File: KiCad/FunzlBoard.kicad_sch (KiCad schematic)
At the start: 0 parts

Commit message: Add main screw holes
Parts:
- added H1, H10, H2, H3, H4, H5, H6, H7, H8, H9: MountingHole, MountingHole:MountingHole_4.3mm_M4_DIN965, symbol Mechanical:MountingHole

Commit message: Cut out for battery
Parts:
- added D1, D10, D11, D12, D13, D14, D15, D16, D17, D18, D19, D2, D20, D21, D22, D23, D24, D25, D26, D27, D28, D29, D3, D30, D31, D32, D33, D34, D35, D36, D37, D38, D39, D4, D40, D41, D42, D43, D44, D5, D6, D7, D8, D9: WS2812B, LED_SMD:LED_WS2812B_PLCC4_5.0x5.0mm_P3.2mm, symbol LED:WS2812B
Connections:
- new net: D22.2 (DOUT), D23.4 (DIN)
- new net: D21.2 (DOUT), D22.4 (DIN)
- new net: D4.2 (DOUT), D5.4 (DIN)
- new net: D3.2 (DOUT), D4.4 (DIN)
- new net: D1.2 (DOUT), D2.4 (DIN)
- new net: D12.2 (DOUT), D13.4 (DIN)
- new net: D11.2 (DOUT), D12.4 (DIN)
- new net: D35.2 (DOUT), D36.4 (DIN)
- new net: D34.2 (DOUT), D35.4 (DIN)
- new net: D20.2 (DOUT), D21.4 (DIN)
- new net: D19.2 (DOUT), D20.4 (DIN)
- new net: D36.2 (DOUT), D37.4 (DIN)
- new net: D8.2 (DOUT), D9.4 (DIN)
- new net: D7.2 (DOUT), D8.4 (DIN)
- new net: D39.2 (DOUT), D40.4 (DIN)
- new net: D38.2 (DOUT), D39.4 (DIN)
- new net: D15.2 (DOUT), D16.4 (DIN)
- new net: D14.2 (DOUT), D15.4 (DIN)
- new net: D40.2 (DOUT), D41.4 (DIN)
- new net: D2.2 (DOUT), D3.4 (DIN)
- new net: D10.4 (DIN), D9.2 (DOUT)
- new net: D18.2 (DOUT), D19.4 (DIN)
- new net: D13.2 (DOUT), D14.4 (DIN)
- new net: D31.2 (DOUT), D32.4 (DIN)
- new net: D30.2 (DOUT), D31.4 (DIN)
- new net: D16.2 (DOUT), D17.4 (DIN)
- new net: D42.2 (DOUT), D43.4 (DIN)
- new net: D41.2 (DOUT), D42.4 (DIN)
- new net: D29.2 (DOUT), D30.4 (DIN)
- new net: D28.2 (DOUT), D29.4 (DIN)
- new net: D10.2 (DOUT), D11.4 (DIN)
- new net: D17.2 (DOUT), D18.4 (DIN)
- new net: D43.2 (DOUT), D44.4 (DIN)
- new net: D37.2 (DOUT), D38.4 (DIN)
- new net: D27.2 (DOUT), D28.4 (DIN)
- new net: D26.2 (DOUT), D27.4 (DIN)
- new net: D6.2 (DOUT), D7.4 (DIN)
- new net: D5.2 (DOUT), D6.4 (DIN)
- new net: D25.2 (DOUT), D26.4 (DIN)
- new net: D24.2 (DOUT), D25.4 (DIN)
- new net: D33.2 (DOUT), D34.4 (DIN)
- new net: D32.2 (DOUT), D33.4 (DIN)
- new net: D23.2 (DOUT), D24.4 (DIN)
- new net +5V: D1.1 (VDD), D10.1 (VDD), D11.1 (VDD), D12.1 (VDD), D13.1 (VDD), D14.1 (VDD), D15.1 (VDD), D16.1 (VDD), D17.1 (VDD), D18.1 (VDD), D19.1 (VDD), D2.1 (VDD), D20.1 (VDD), D21.1 (VDD), D22.1 (VDD), D23.1 (VDD), D24.1 (VDD), D25.1 (VDD), D26.1 (VDD), D27.1 (VDD), D28.1 (VDD), D29.1 (VDD), D3.1 (VDD), D30.1 (VDD), D31.1 (VDD), D32.1 (VDD), D33.1 (VDD), D34.1 (VDD), D35.1 (VDD), D36.1 (VDD), D37.1 (VDD), D38.1 (VDD), D39.1 (VDD), D4.1 (VDD), D40.1 (VDD), D41.1 (VDD), D42.1 (VDD), D43.1 (VDD), D44.1 (VDD), D5.1 (VDD), D6.1 (VDD), D7.1 (VDD), D8.1 (VDD), D9.1 (VDD)
- new net GND: D1.3 (VSS), D10.3 (VSS), D11.3 (VSS), D12.3 (VSS), D13.3 (VSS), D14.3 (VSS), D15.3 (VSS), D16.3 (VSS), D17.3 (VSS), D18.3 (VSS), D19.3 (VSS), D2.3 (VSS), D20.3 (VSS), D21.3 (VSS), D22.3 (VSS), D23.3 (VSS), D24.3 (VSS), D25.3 (VSS), D26.3 (VSS), D27.3 (VSS), D28.3 (VSS), D29.3 (VSS), D3.3 (VSS), D30.3 (VSS), D31.3 (VSS), D32.3 (VSS), D33.3 (VSS), D34.3 (VSS), D35.3 (VSS), D36.3 (VSS), D37.3 (VSS), D38.3 (VSS), D39.3 (VSS), D4.3 (VSS), D40.3 (VSS), D41.3 (VSS), D42.3 (VSS), D43.3 (VSS), D44.3 (VSS), D5.3 (VSS), D6.3 (VSS), D7.3 (VSS), D8.3 (VSS), D9.3 (VSS)

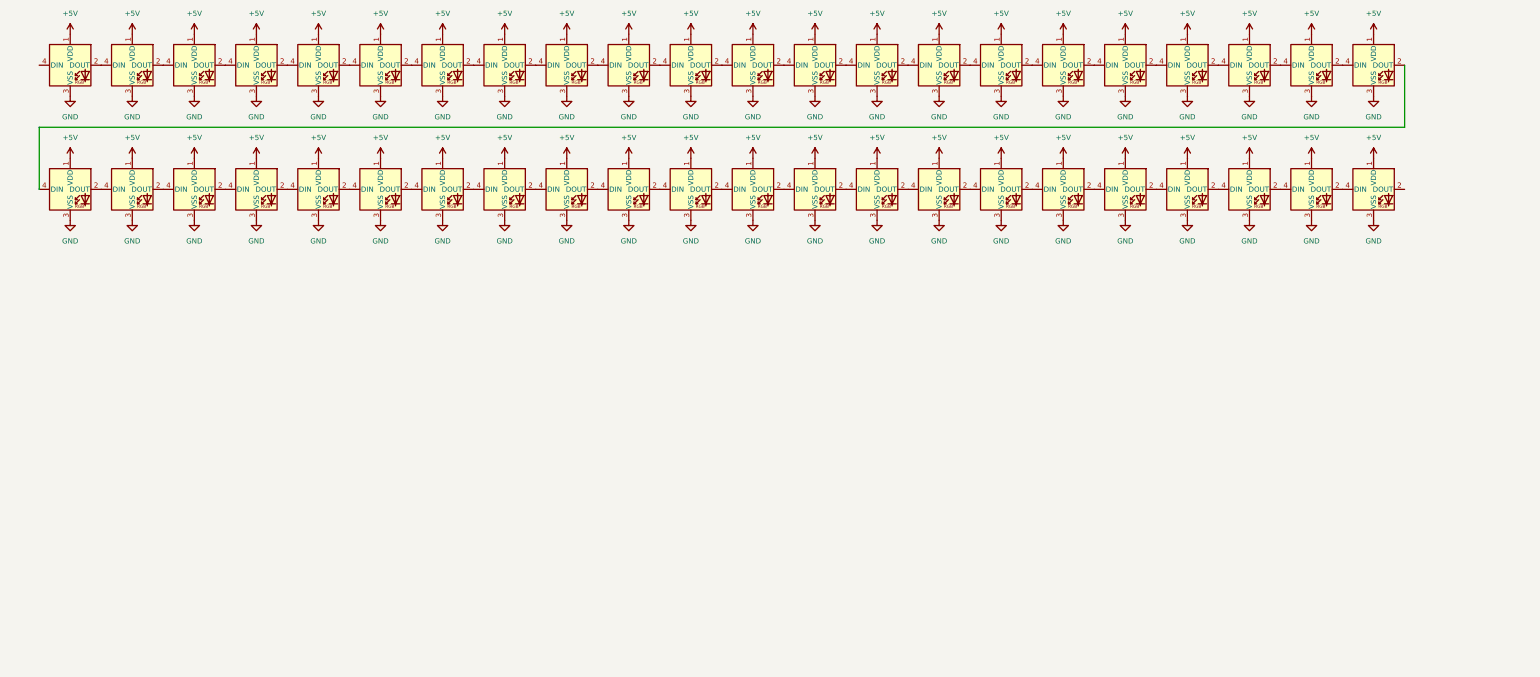
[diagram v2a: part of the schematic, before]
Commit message: Align LEDs on main board
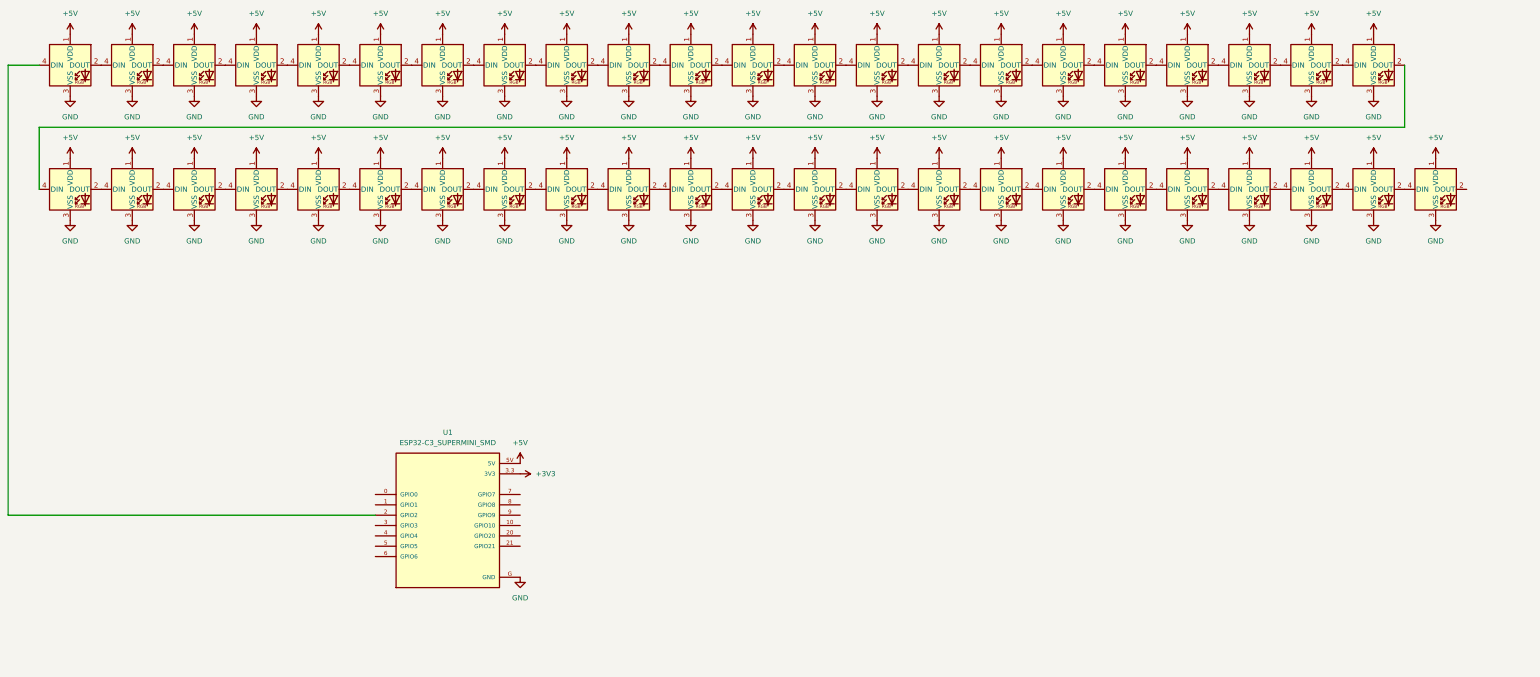
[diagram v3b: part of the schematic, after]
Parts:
- added D45: WS2812B, LED_SMD:LED_WS2812B_PLCC4_5.0x5.0mm_P3.2mm, symbol LED:WS2812B
- added U1: ESP32-C3_SUPERMINI_SMD, Lib:MODULE_ESP32-C3_SUPERMINI, symbol FunzlBoard:ESP32-C3_SUPERMINI_SMD
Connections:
- net +5V: now also D45.1 (VDD), U1.5V
- net GND: now also D45.3 (VSS), U1.G (GND)
- net at D1.4 (DIN): now also U1.2 (GPIO2)
- net at D44.2 (DOUT): now also D45.4 (DIN)
- new net +3V3: U1.3.3 (3V3)

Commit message: .
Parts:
- removed D44, D45: WS2812B, LED_SMD:LED_WS2812B_PLCC4_5.0x5.0mm_P3.2mm, symbol LED:WS2812B

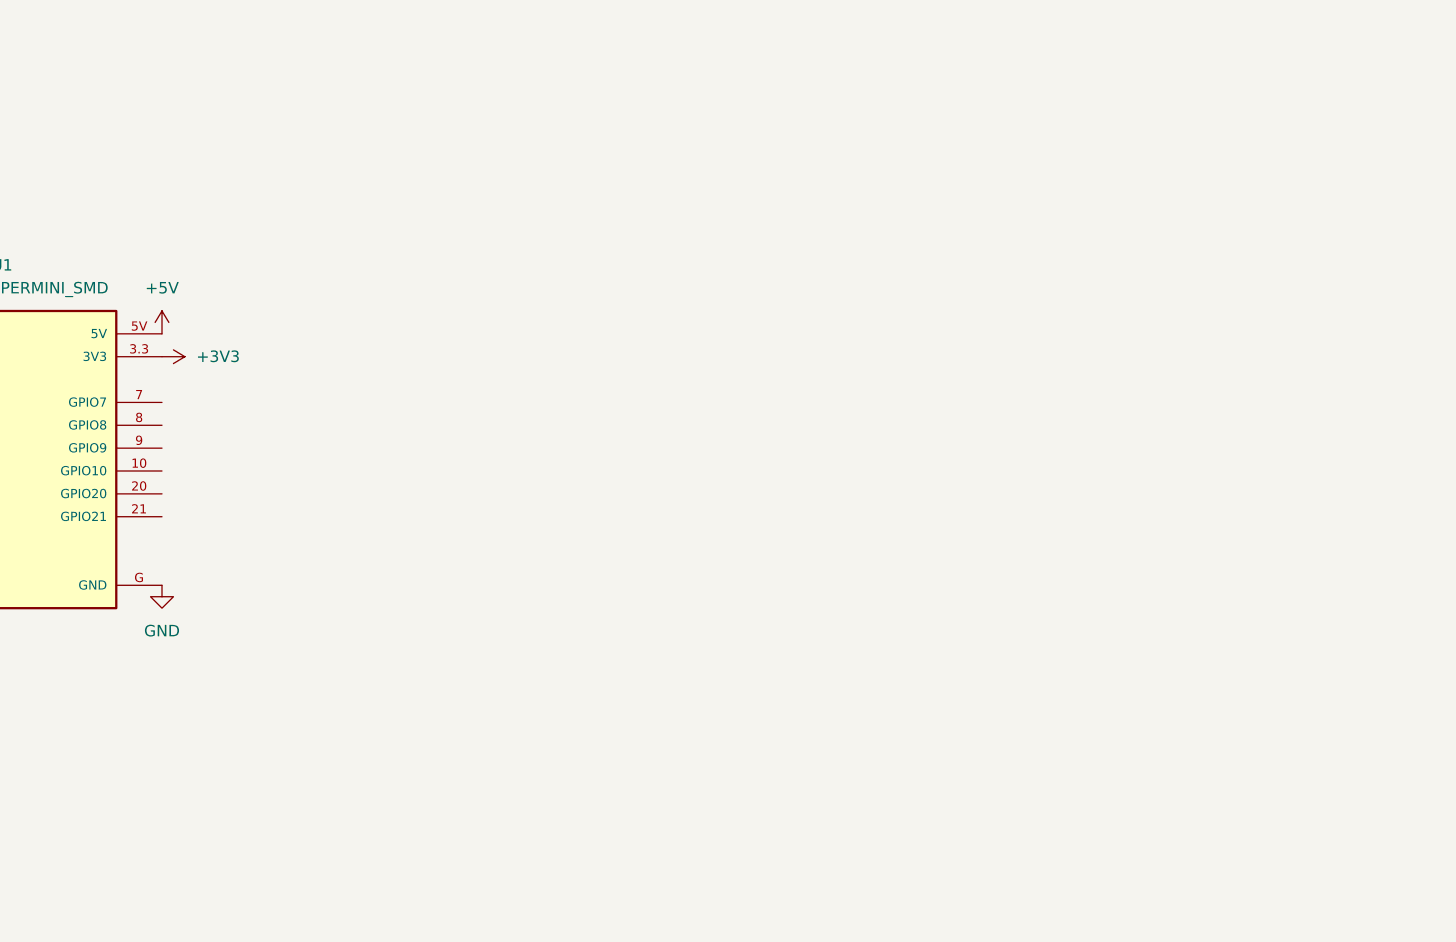
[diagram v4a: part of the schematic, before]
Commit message: Cut out board for components
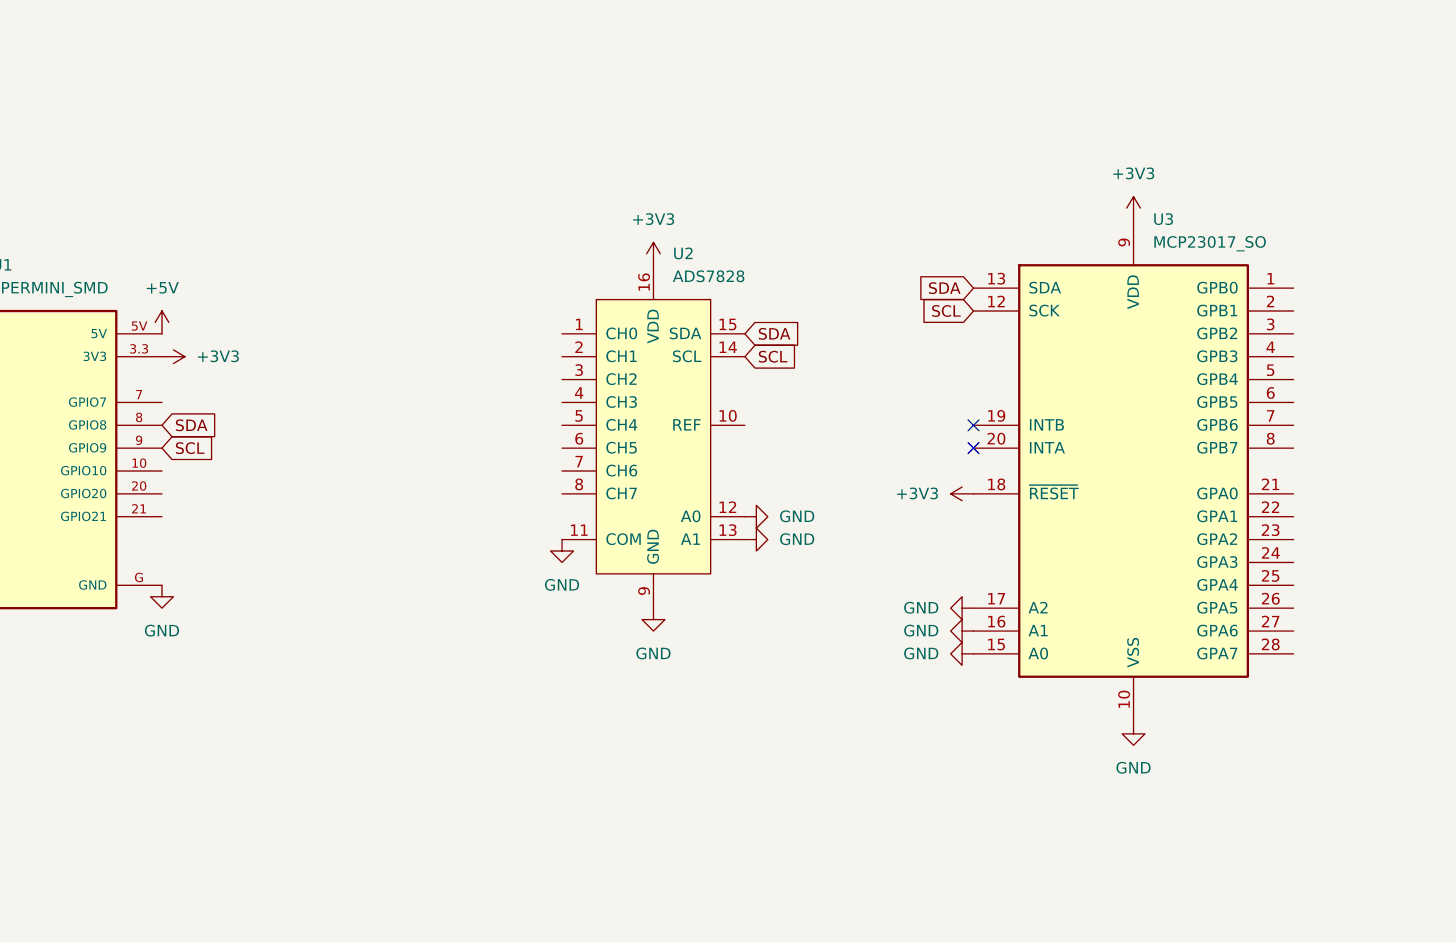
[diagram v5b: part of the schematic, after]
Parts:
- added U2: ADS7828, Package_SO:TSSOP-16_4.4x5mm_P0.65mm, symbol Analog_ADC:ADS7828
- added U3: MCP23017_SO, Package_SO:SOIC-28W_7.5x17.9mm_P1.27mm, symbol Interface_Expansion:MCP23017_SO
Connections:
- net +3V3: now also U2.16 (VDD), U3.18 (~{RESET}), U3.9 (VDD)
- net GND: now also U2.11 (COM), U2.12 (A0), U2.13 (A1), U2.9 (GND), U3.10 (VSS), U3.15 (A0), U3.16 (A1), U3.17 (A2)
- net SDA: now reaches U1.8 (GPIO8)
- net SDA: now also U2.15 (SDA), U3.13 (SDA)
- net SCL: now reaches U1.9 (GPIO9)
- net SCL: now also U2.14 (SCL), U3.12 (SCK)
- no-connect marks 0 -> 2

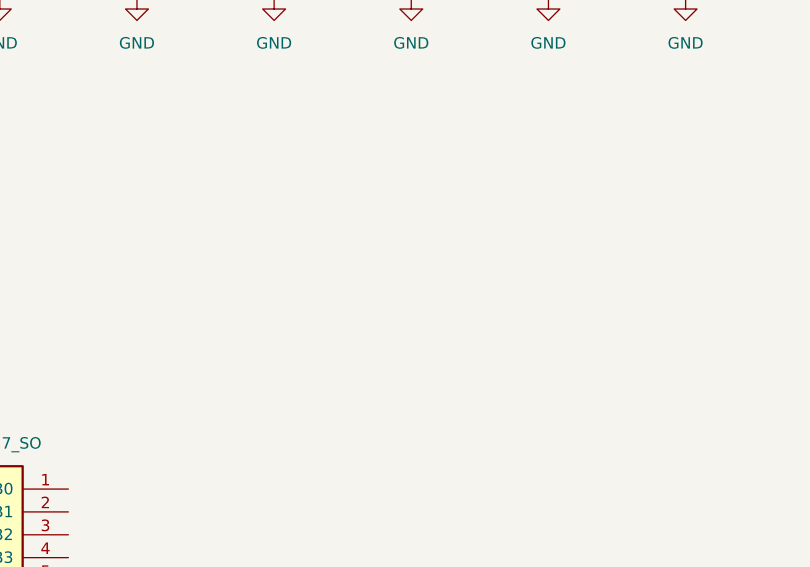
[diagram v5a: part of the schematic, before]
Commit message: Add Color Buttons to PCB
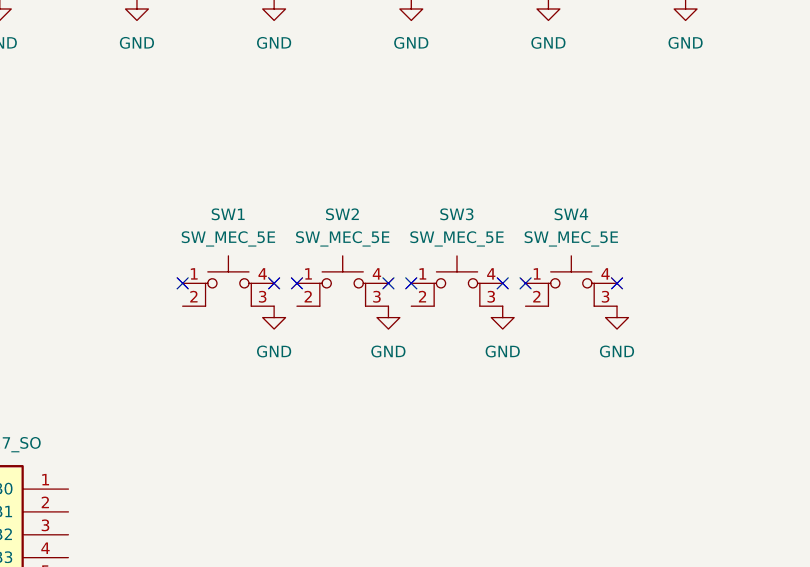
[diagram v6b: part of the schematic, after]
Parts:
- added SW1, SW2, SW3, SW4: SW_MEC_5E, Lib:ColorButton, symbol Switch:SW_MEC_5E
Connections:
- net GND: now also SW1.3 (K), SW2.3 (K), SW3.3 (K), SW4.3 (K)
- no-connect marks 2 -> 10

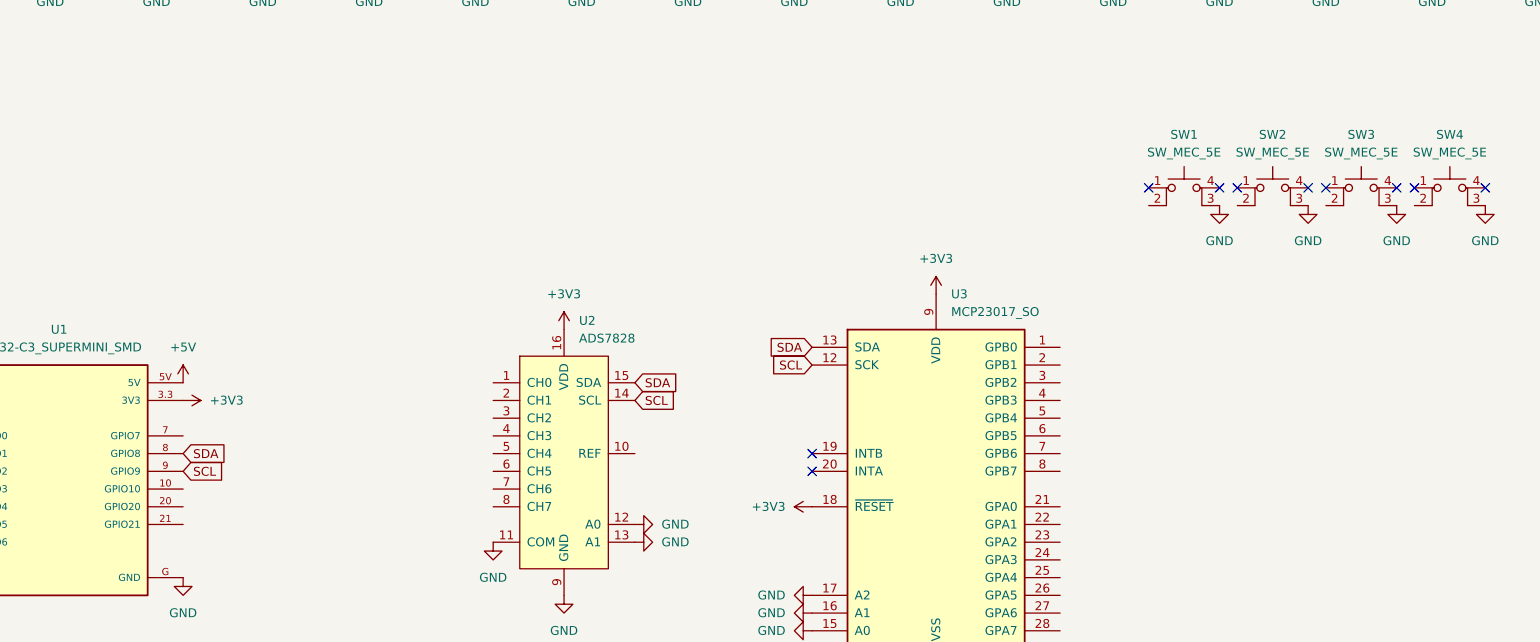
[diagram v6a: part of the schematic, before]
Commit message: Add footprints for sliders
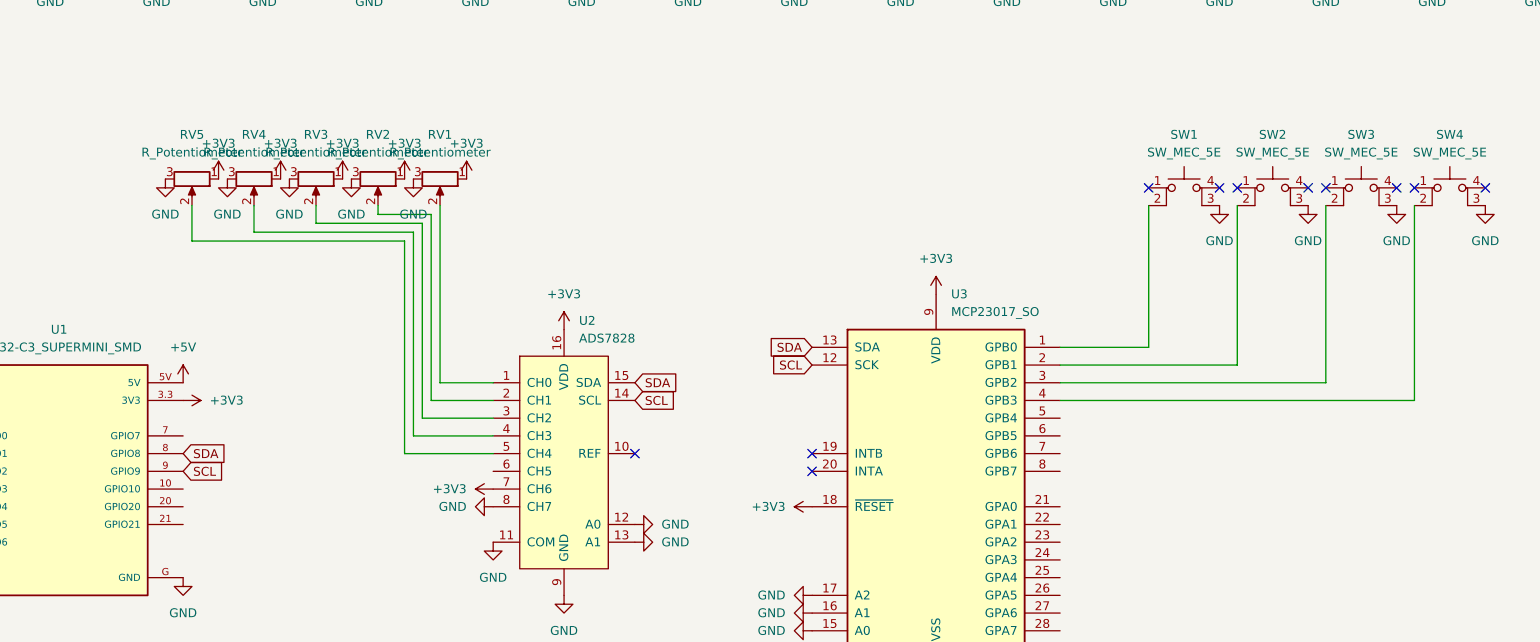
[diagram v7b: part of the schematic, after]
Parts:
- added RV1, RV2, RV3: R_Potentiometer, Lib:Slider, symbol Device:R_Potentiometer
- added RV4, RV5: R_Potentiometer, symbol Device:R_Potentiometer
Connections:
- net +3V3: now also U2.7 (CH6), RV1.1, RV2.1, RV3.1, RV4.1, RV5.1
- net GND: now also U2.8 (CH7), RV1.3, RV2.3, RV3.3, RV4.3, RV5.3
- net at U2.1 (CH0): now also RV1.2
- net at U2.2 (CH1): now also RV2.2
- net at U2.3 (CH2): now also RV3.2
- net at U2.4 (CH3): now also RV4.2
- net at U2.5 (CH4): now also RV5.2
- net at SW1.2: now also U3.1 (GPB0)
- net at SW4.2: now also U3.4 (GPB3)
- net at U3.2 (GPB1): now also SW2.2
- net at U3.3 (GPB2): now also SW3.2
- no-connect marks 10 -> 11
